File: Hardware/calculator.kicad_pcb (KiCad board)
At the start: 2 copper layers, 72 x 138 mm, 49 parts, among them J1 Sharp_LCD_10Pin

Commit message: refactor: use activeAnnunciators for display rendering and add miscellaneous hardware support files
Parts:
- added C10 (x3): C_0402_1005Metric, C_0402_1005Metric, F.Cu at (35.0, -108.0)
- added C11 (x3): C_0402_1005Metric, C_0402_1005Metric, F.Cu at (45.0, -108.0)
- added C12 (x3): C_0402_1005Metric, C_0402_1005Metric, F.Cu at (55.0, -108.0)
- moved B22 6.57 mm to (32.7, -42.0)
- moved B23 6.57 mm to (32.7, -32.0)
- moved B24 6.57 mm to (32.7, -22.0)
- moved B25 6.57 mm to (32.7, -12.0)
- moved B26 4.38 mm to (46.4, -42.0)
- moved B27 4.38 mm to (46.4, -32.0)
- moved B28 4.38 mm to (46.4, -22.0)
- moved B29 4.38 mm to (46.4, -12.0)
- moved B30 2.19 mm to (60.1, -42.0)
- moved B31 2.19 mm to (60.1, -32.0)
- moved B32 2.19 mm to (60.1, -22.0)
- moved B33 2.19 mm to (60.1, -12.0)
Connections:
- J1 pad 1: P21 -> Net-(J1-Pad1)
- J1 pad 10: GND -> Net-(J1-Pad10)
- J1 pad 2: P20 -> Net-(J1-Pad2)
- J1 pad 3: P19 -> Net-(J1-Pad3)
- J1 pad 4: P18 -> Net-(J1-Pad4)
- J1 pad 5: GND -> Net-(J1-Pad5)
- J1 pad 6: VCC -> +3V3
- J1 pad 7: VCC -> GND
- J1 pad 8: GND -> Net-(J1-Pad8)
- J1 pad 9: GND -> Net-(J1-Pad9)
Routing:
- net P21: track 0.00 -> 217.1 mm, vias 0 -> 2
- net P10: track 0.00 -> 181.6 mm, vias 0 -> 3
- net P6: track 0.00 -> 163.4 mm, vias 0 -> 4
- net P14: track 0.00 -> 155.5 mm, vias 0 -> 1
- net P5: track 0.00 -> 155.1 mm, vias 0 -> 5
- net P15: track 0.00 -> 154.5 mm, vias 0 -> 1
- net P0: track 0.00 -> 137.9 mm, vias 0 -> 4
- net P7: track 0.00 -> 130.9 mm, vias 0 -> 1
- net P9: track 0.00 -> 130.3 mm, vias 0 -> 1
- net P8: track 0.00 -> 128.4 mm, vias 0 -> 1
- net P20: track 0.00 -> 123.8 mm, vias 0 -> 2
- net P4: track 0.00 -> 113.2 mm, vias 0 -> 6
- net P16: track 0.00 -> 109.4 mm, vias 0 -> 1
- net P1: track 0.00 -> 105.0 mm, vias 0 -> 4
- net P18: track 0.00 -> 47.8 mm, vias 0 -> 1
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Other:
- board size 72 x 138 mm -> 71 x 138 mm
- board text added: "Active Area"
- board text added: "Boss L"
- board text added: "Boss R"
- board text added: "CR2032 Bucket"
- board text added: "Chassis Cavity"
- board text added: "ERC13265FS-1 (2.5")"
- board text added: "LCD Glass"
- board text removed: "SHARP LS027B7DH01"

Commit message: refactor: remove tactile switches from PCB and update hardware manufacturing and UI scripts
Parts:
- J1: value Sharp_LCD_10Pin -> Hirose_FH12-28S-0.5SH_1x28-1MP_P0.50mm_Horizontal; footprint Connector_FFC-FPC:Hirose_FH12-10S-0.5SH_1x10-1MP_P0.50mm_Horizontal -> Hirose_FH12-28S-0.5SH_1x28-1MP_P0.50mm_Horizontal; moved to B.Cu
- moved J1 18.5 mm to (45.0, -92.0)
- turned MCU1 to -90 degrees
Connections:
- J1 pad 1: Net-(J1-Pad1) -> (no net)
- J1 pad 10: Net-(J1-Pad10) -> (no net)
- J1 pad 2: Net-(J1-Pad2) -> (no net)
- J1 pad 3: Net-(J1-Pad3) -> (no net)
- J1 pad 4: Net-(J1-Pad4) -> (no net)
- J1 pad 5: Net-(J1-Pad5) -> (no net)
- J1 pad 6: +3V3 -> (no net)
- J1 pad 7: GND -> (no net)
- J1 pad 8: Net-(J1-Pad8) -> (no net)
- J1 pad 9: Net-(J1-Pad9) -> (no net)
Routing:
- net P3: track 0.00 -> 39.5 mm, vias 0 -> 1
- net P19: track 39.5 -> 0.00 mm, vias 1 -> 0
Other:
- outline, holes or cut-outs redrawn

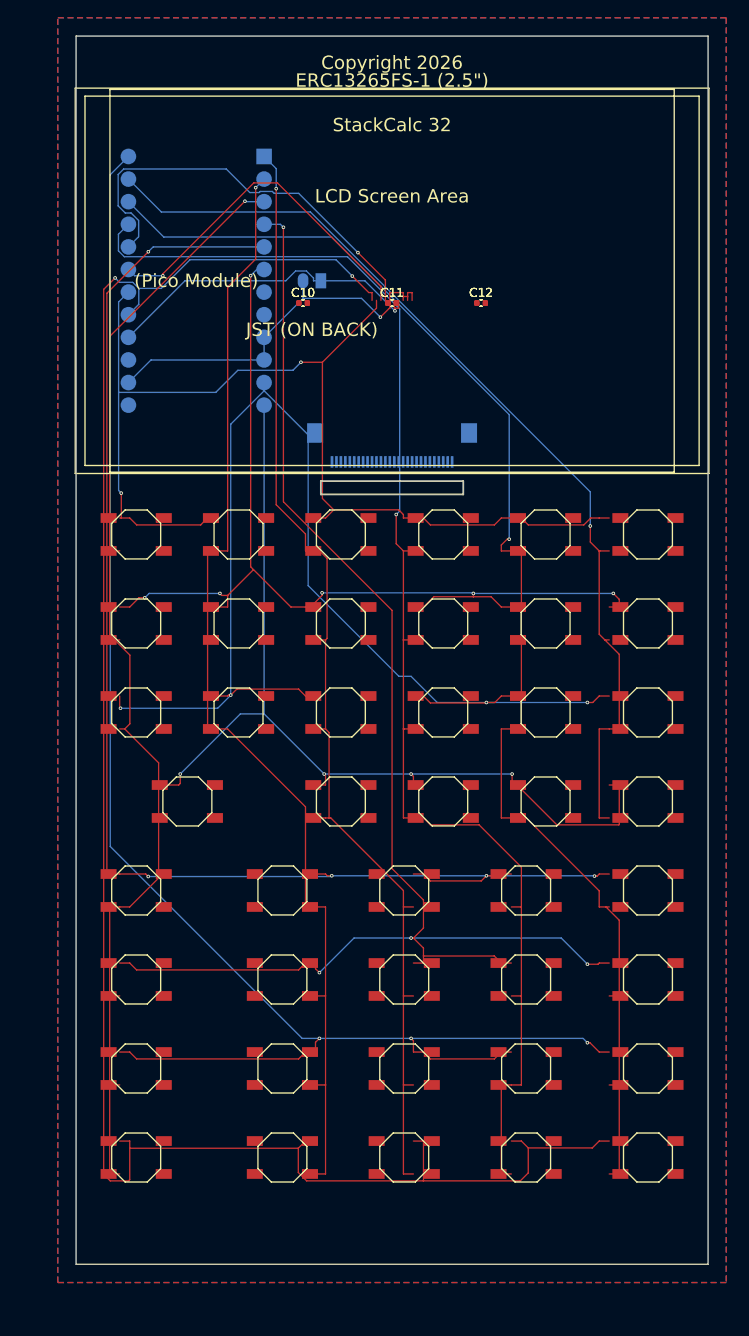
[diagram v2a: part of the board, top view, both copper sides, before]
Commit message: feat: update hardware routing and footprint layout with supporting utility scripts and firmware integration
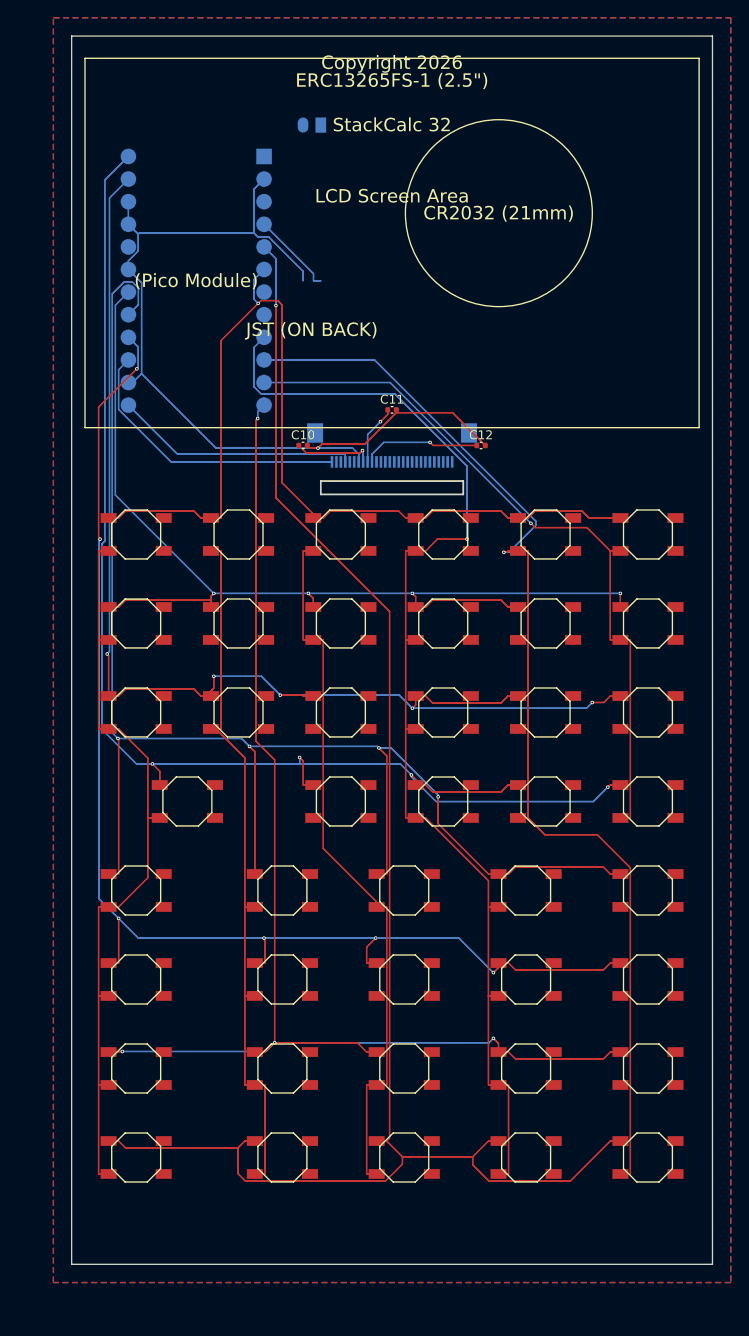
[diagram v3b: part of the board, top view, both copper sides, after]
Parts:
- removed the C10 at (35.0, -108.0) (x2)
- removed the C11 at (45.0, -108.0) (x2)
- removed the C12 at (55.0, -108.0) (x2)
- moved JST1 17.5 mm to (36.0, -128.0)
- moved C10 16.0 mm to (35.0, -92.0)
- moved C12 16.0 mm to (55.0, -92.0)
- moved C11 12.0 mm to (45.0, -96.0)
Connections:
- J1 pad 1: (no net) -> Net-(J1-Pad1)
- J1 pad 10: (no net) -> Net-(J1-Pad10)
- J1 pad 2: (no net) -> Net-(J1-Pad2)
- J1 pad 3: (no net) -> Net-(J1-Pad3)
- J1 pad 4: (no net) -> Net-(J1-Pad4)
- J1 pad 5: (no net) -> Net-(J1-Pad5)
- J1 pad 6: (no net) -> +3V3
- J1 pad 7: (no net) -> GND
- J1 pad 8: (no net) -> Net-(J1-Pad8)
- J1 pad 9: (no net) -> Net-(J1-Pad9)
- MCU1 pad 18: P3 -> GND
- MCU1 pad 22: P7 -> Net-(J1-Pad1)
- MCU1 pad 23: P8 -> GND
- MCU1 pad 24: P9 -> Net-(J1-Pad4)
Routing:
- net P1: track 105.0 -> 298.8 mm
- net P5: track 155.1 -> 338.7 mm, vias 5 -> 4
- net GND: track 44.9 -> 206.6 mm
- net P21: track 217.1 -> 364.1 mm, vias 2 -> 1
- net P0: track 137.9 -> 278.0 mm, vias 4 -> 5
- net P6: track 163.4 -> 286.7 mm, vias 4 -> 6
- net P4: track 113.2 -> 230.6 mm, vias 6 -> 4
- net P10: track 181.6 -> 294.8 mm, vias 3 -> 4
- net P15: track 154.5 -> 264.8 mm
- net P14: track 155.5 -> 264.5 mm
- net P20: track 123.8 -> 217.2 mm, vias 2 -> 1
- net Net-(J1-Pad1): track 0.00 -> 64.9 mm
- net P16: track 109.4 -> 164.7 mm
- net Net-(J1-Pad4): track 0.00 -> 55.1 mm
- net P18: track 47.8 -> 0.00 mm, vias 1 -> 0
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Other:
- board size 71 x 138 mm -> 72 x 138 mm
- board text added: "CR2032 (21mm)"
- board text added: "LCD Glass Boundary (69x41.5)"
- board text removed: "CR2032 Bucket"
